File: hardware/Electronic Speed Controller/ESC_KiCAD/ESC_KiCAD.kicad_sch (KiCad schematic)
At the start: 0 parts

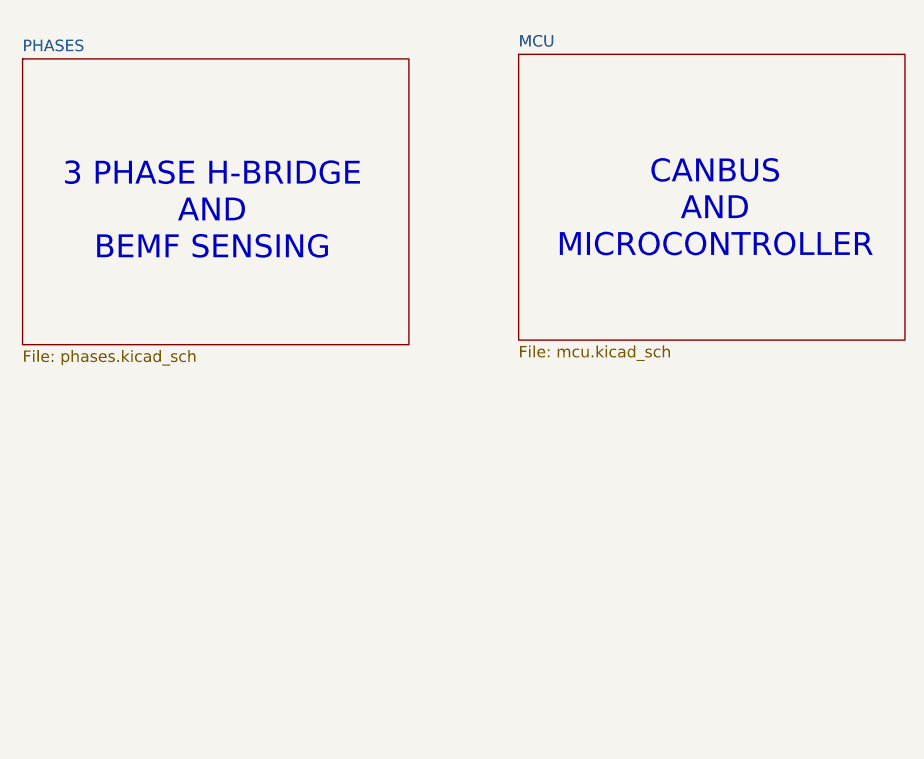
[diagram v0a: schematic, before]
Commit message: esc sensing circuitry
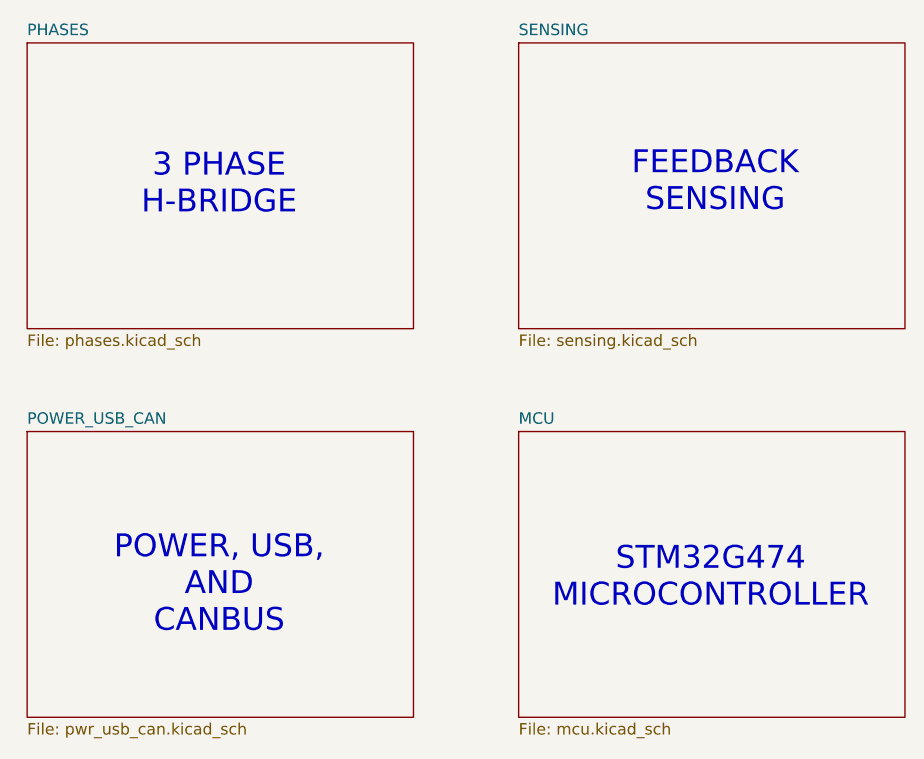
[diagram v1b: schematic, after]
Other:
- added sheet POWER_USB_CAN (pwr_usb_can.kicad_sch)
- added sheet SENSING (sensing.kicad_sch)
- note added: "3 PHASE H-BRIDGE"
- note added: "FEEDBACK SENSING"
- note added: "POWER, USB, AND CANBUS"
- note added: "STM32G474 MICROCONTROLLER"
- note removed: "3 PHASE H-BRIDGE AND BEMF SENSING"
- note removed: "CANBUS AND MICROCONTROLLER"
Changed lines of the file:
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@@
 		(comment 5 "SIGNED:")
 	)
-	(text "CANBUS\nAND\nMICROCONTROLLER"
+	(text "POWER, USB,\nAND\nCANBUS"
 		(exclude_from_sim no)
-		(at 171.704 96.012 0)
+		(at 116.586 137.668 0)
 		(effects
 			(font
@@
 		)
 	)
-	(text "3 PHASE H-BRIDGE\nAND\nBEMF SENSING"
+	(text "STM32G474\nMICROCONTROLLER"
 		(exclude_from_sim no)
-		(at 115.824 96.266 0)
+		(at 171.196 136.906 0)
+		(effects
+			(font
+				(size 2.54 2.54)
+			)
+		)
+	)
+	(text "3 PHASE\nH-BRIDGE"
+		(exclude_from_sim no)
+		(at 116.586 93.218 0)
+		(effects
+			(font
+				(size 2.54 2.54)
+			)
+		)
+	)
+	(text "FEEDBACK\nSENSING\n\n"
+		(exclude_from_sim no)
+		(at 171.704 94.996 0)
 		(effects
 			(font
@@
 	)
 	(sheet
-		(at 149.86 78.74)
+		(at 149.86 120.65)
 		(size 42.926 31.75)
 		(fields_autoplaced yes)
@@
 		)
 		(property "Sheetname" "MCU"
-			(at 149.86 78.0284 0)
+			(at 149.86 119.9384 0)
 			(effects
 				(font
@@
 		)
 		(property "Sheetfile" "mcu.kicad_sch"
-			(at 149.86 111.0746 0)
+			(at 149.86 152.9846 0)
+			(effects
+				(font
+					(size 1.27 1.27)
+				)
+				(justify left top)
+			)
+		)
+		(instances
+			(project "ESC_KiCAD"
+				(path "/befe2457-67b1-4e2c-96c1-c48eafddae5c"
+					(page "5")
+				)
+			)
+		)
+	)
+	(sheet
+		(at 95.25 120.65)
+		(size 42.926 31.75)
+		(fields_autoplaced yes)
+		(stroke
+			(width 0.1524)
+			(type solid)
+		)
+		(fill
+			(color 0 0 0 0.0000)
+		)
+		(property "Sheetname" "POWER_USB_CAN"
+			(at 95.25 119.9384 0)
+			(effects
+				(font
+					(size 1.27 1.27)
+				)
+				(justify left bottom)
+			)
+		)
+		(property "Sheetfile" "pwr_usb_can.kicad_sch"
+			(at 95.25 152.9846 0)
+			(effects
+				(font
+					(size 1.27 1.27)
+				)
+				(justify left top)
+			)
+		)
+		(instances
+			(project "ESC_KiCAD"
+				(path "/befe2457-67b1-4e2c-96c1-c48eafddae5c"
+					(page "4")
+				)
+			)
+		)
+	)
+	(sheet
+		(at 149.86 77.47)
+		(size 42.926 31.75)
+		(fields_autoplaced yes)
+		(stroke
+			(width 0.1524)
+			(type solid)
+		)
+		(fill
+			(color 0 0 0 0.0000)
+		)
+		(property "Sheetname" "SENSING"
+			(at 149.86 76.7584 0)
+			(effects
+				(font
+					(size 1.27 1.27)
+				)
+				(justify left bottom)
+			)
+		)
+		(property "Sheetfile" "sensing.kicad_sch"
+			(at 149.86 109.8046 0)
 			(effects
 				(font
@@
 	)
 	(sheet
-		(at 94.742 79.248)
+		(at 95.25 77.47)
 		(size 42.926 31.75)
 		(fields_autoplaced yes)
@@
 		)
 		(property "Sheetname" "PHASES"
-			(at 94.742 78.5364 0)
+			(at 95.25 76.7584 0)
 			(effects
 				(font
@@
 		)
 		(property "Sheetfile" "phases.kicad_sch"
-			(at 94.742 111.5826 0)
+			(at 95.25 109.8046 0)
 			(effects
 				(font

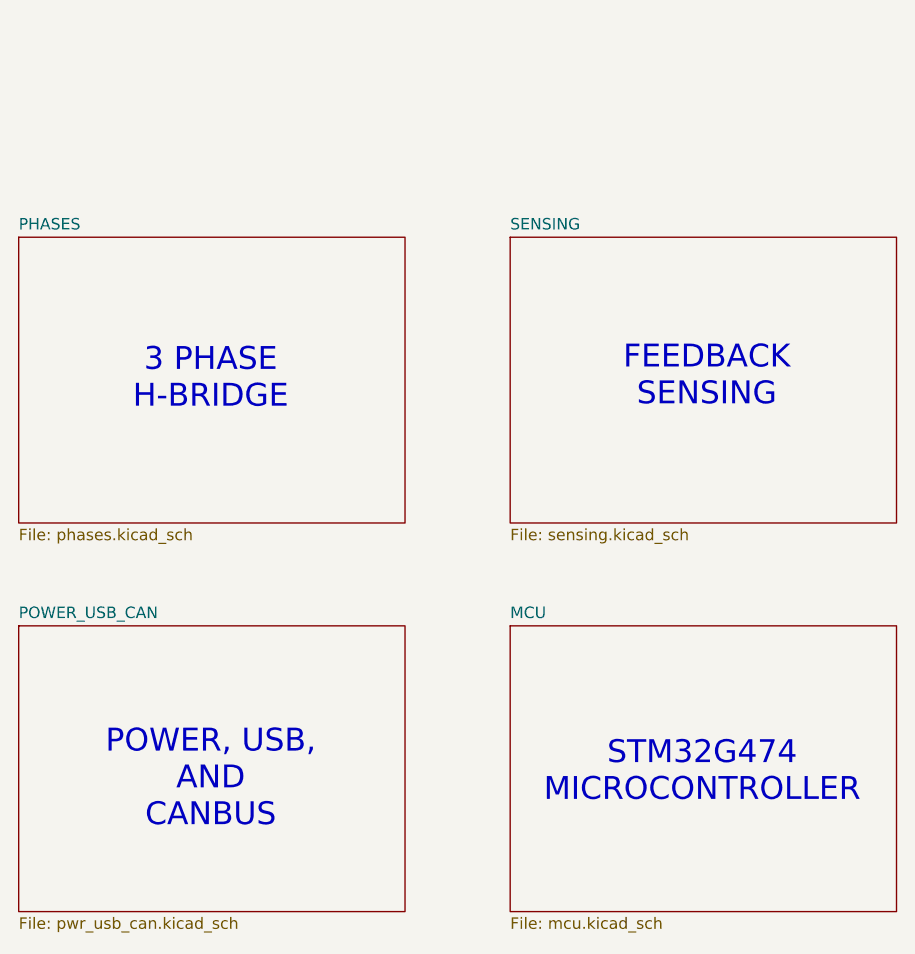
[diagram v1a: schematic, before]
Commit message: change drivers to C++, add software IIR filtering, improve GCS software
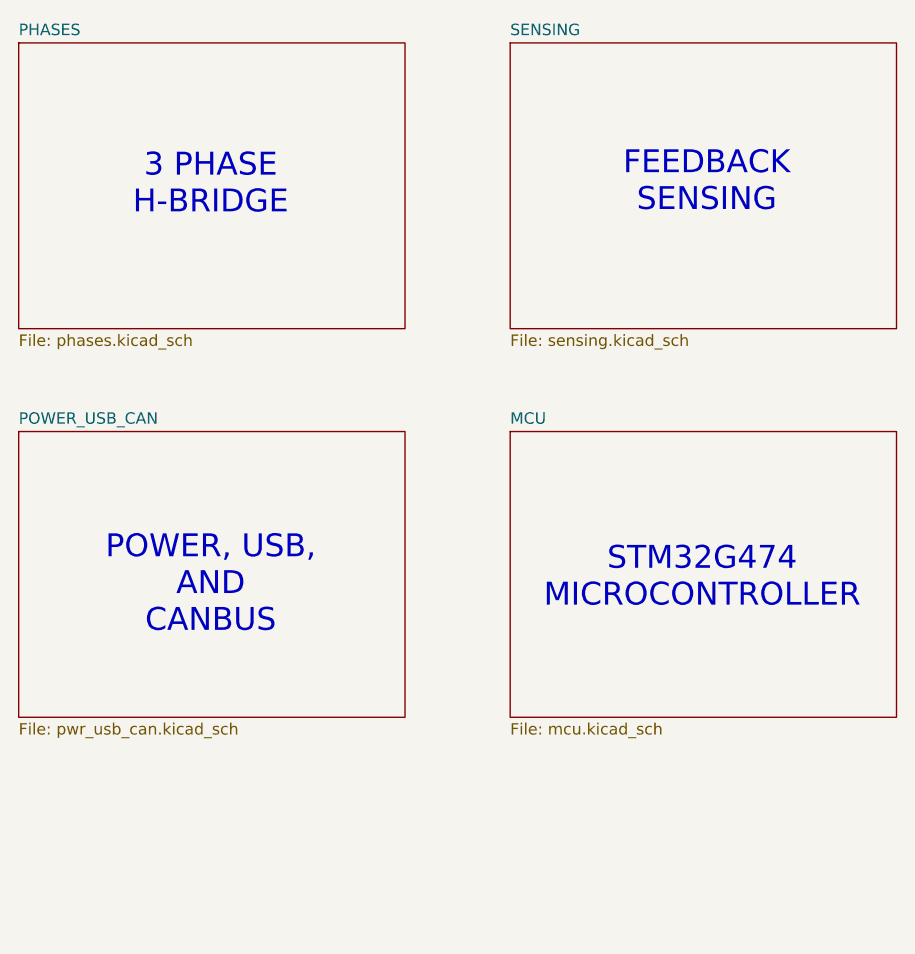
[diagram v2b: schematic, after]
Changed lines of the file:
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@@
 	(text "POWER, USB,\nAND\nCANBUS"
 		(exclude_from_sim no)
-		(at 116.586 137.668 0)
+		(at 116.586 116.078 0)
 		(effects
 			(font
@@
 	(text "STM32G474\nMICROCONTROLLER"
 		(exclude_from_sim no)
-		(at 171.196 136.906 0)
+		(at 171.196 115.316 0)
 		(effects
 			(font
@@
 	(text "3 PHASE\nH-BRIDGE"
 		(exclude_from_sim no)
-		(at 116.586 93.218 0)
+		(at 116.586 71.628 0)
 		(effects
 			(font
@@
 	(text "FEEDBACK\nSENSING\n\n"
 		(exclude_from_sim no)
-		(at 171.704 94.996 0)
+		(at 171.704 73.406 0)
 		(effects
 			(font
@@
 	)
 	(sheet
-		(at 149.86 120.65)
+		(at 149.86 99.06)
 		(size 42.926 31.75)
 		(fields_autoplaced yes)
@@
 		)
 		(property "Sheetname" "MCU"
-			(at 149.86 119.9384 0)
+			(at 149.86 98.3484 0)
 			(effects
 				(font
@@
 		)
 		(property "Sheetfile" "mcu.kicad_sch"
-			(at 149.86 152.9846 0)
+			(at 149.86 131.3946 0)
 			(effects
 				(font
@@
 	)
 	(sheet
-		(at 95.25 120.65)
+		(at 95.25 99.06)
 		(size 42.926 31.75)
 		(fields_autoplaced yes)
@@
 		)
 		(property "Sheetname" "POWER_USB_CAN"
-			(at 95.25 119.9384 0)
+			(at 95.25 98.3484 0)
 			(effects
 				(font
@@
 		)
 		(property "Sheetfile" "pwr_usb_can.kicad_sch"
-			(at 95.25 152.9846 0)
+			(at 95.25 131.3946 0)
 			(effects
 				(font
@@
 	)
 	(sheet
-		(at 149.86 77.47)
+		(at 149.86 55.88)
 		(size 42.926 31.75)
 		(fields_autoplaced yes)
@@
 		)
 		(property "Sheetname" "SENSING"
-			(at 149.86 76.7584 0)
+			(at 149.86 55.1684 0)
 			(effects
 				(font
@@
 		)
 		(property "Sheetfile" "sensing.kicad_sch"
-			(at 149.86 109.8046 0)
+			(at 149.86 88.2146 0)
 			(effects
 				(font
@@
 	)
 	(sheet
-		(at 95.25 77.47)
+		(at 95.25 55.88)
 		(size 42.926 31.75)
 		(fields_autoplaced yes)
@@
 		)
 		(property "Sheetname" "PHASES"
-			(at 95.25 76.7584 0)
+			(at 95.25 55.1684 0)
 			(effects
 				(font
@@
 		)
 		(property "Sheetfile" "phases.kicad_sch"
-			(at 95.25 109.8046 0)
+			(at 95.25 88.2146 0)
 			(effects
 				(font

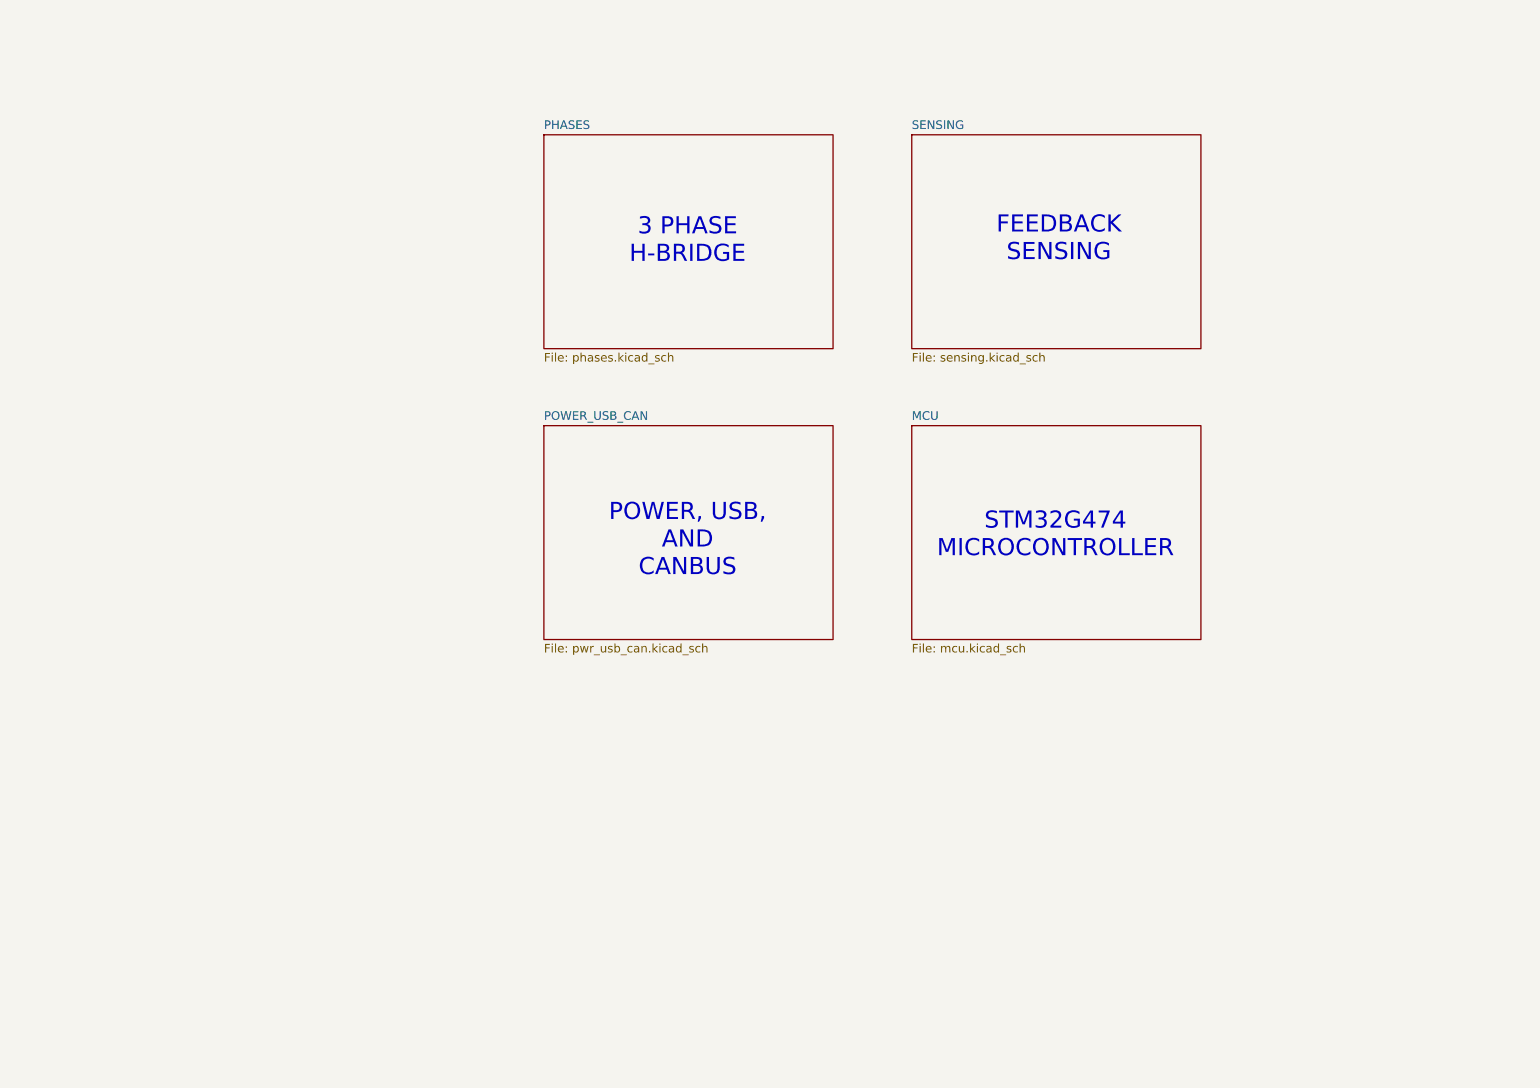
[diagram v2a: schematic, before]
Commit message: finish ESC hardware RevA, CC2500 driver working
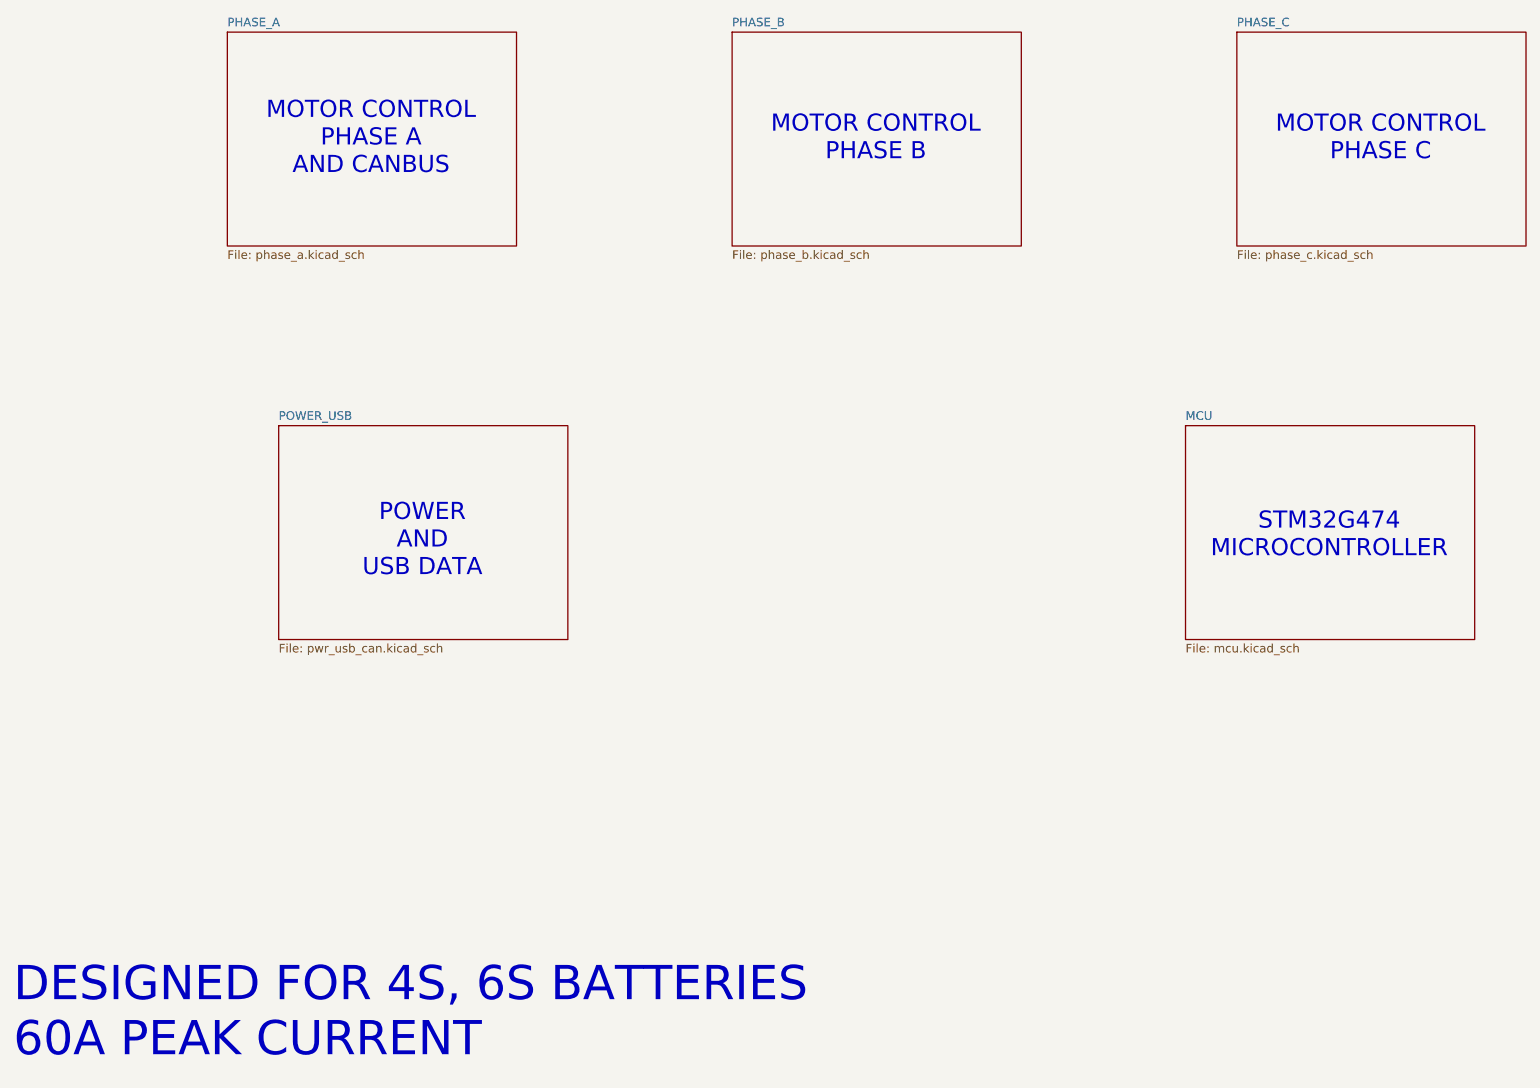
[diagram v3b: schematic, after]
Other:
- sheet PHASES renamed PHASE_A
- sheet POWER_USB_CAN renamed POWER_USB
- removed sheet SENSING
- added sheet PHASE_B (phase_b.kicad_sch)
- added sheet PHASE_C (phase_c.kicad_sch)
- sheet PHASE_A: file phases.kicad_sch -> phase_a.kicad_sch
- note added: "DESIGNED FOR 4S, 6S BATTERIES 60A PEAK CURRENT"
- note added: "MOTOR CONTROL PHASE A AND CANBUS"
- note added: "MOTOR CONTROL PHASE B"
- note added: "MOTOR CONTROL PHASE C"
- note added: "POWER AND USB DATA"
- note removed: "3 PHASE H-BRIDGE"
- note removed: "FEEDBACK SENSING"
- note removed: "POWER, USB, AND CANBUS"
